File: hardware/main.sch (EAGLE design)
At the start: 104 parts, among them IC1 MPU-6050, IC2 TB6612FNG, M1 MOTOR_MOUNT_V2, M2 LED_MOUNT, M3 LED_MOUNT, M4 LED_MOUNT, M5 LED_MOUNT, M6 LED_MOUNT, M7 LED_MOUNT, Q7 IRLML2244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

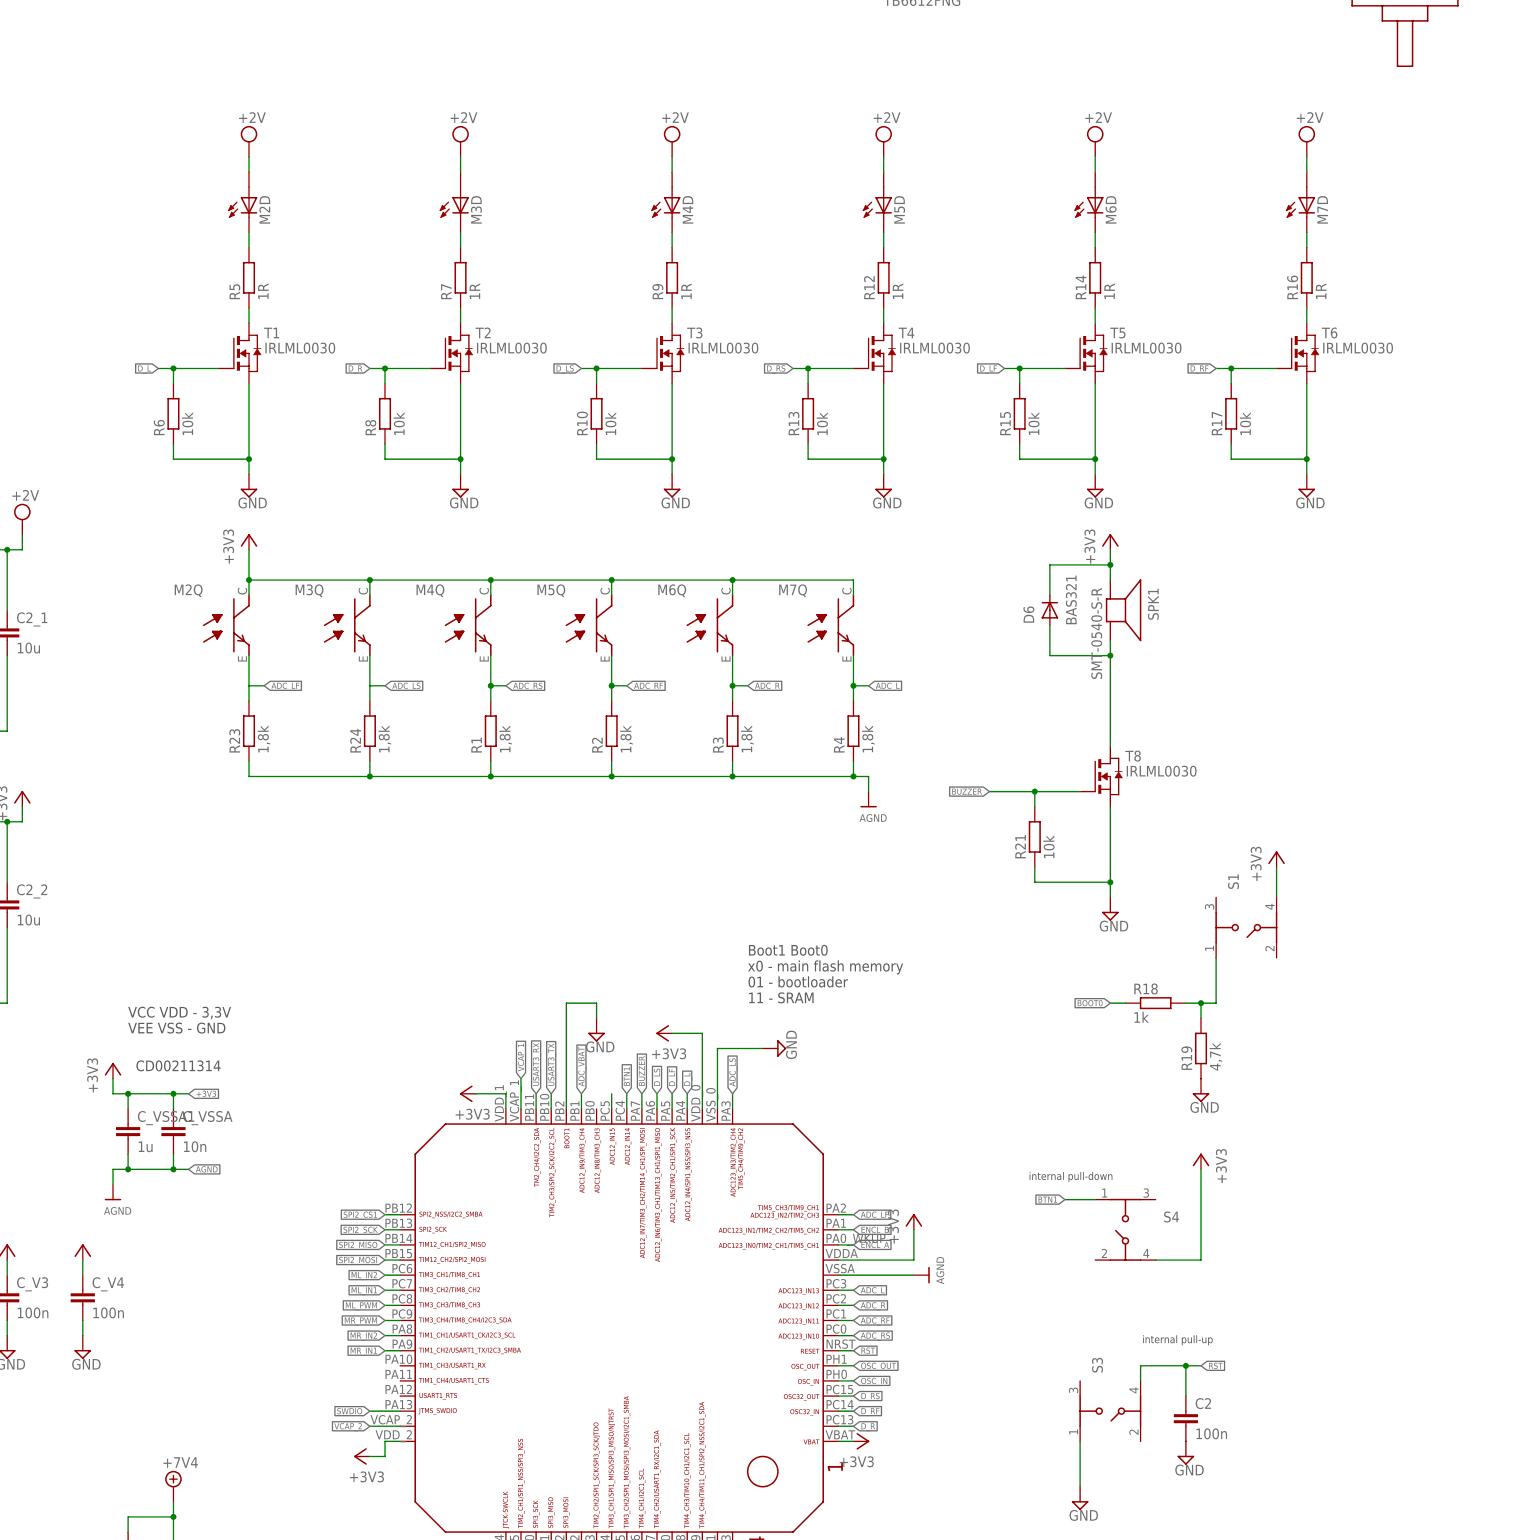
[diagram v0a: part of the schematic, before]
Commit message: Rozmieszczone diody na dziobie, przelotki przy DCDC
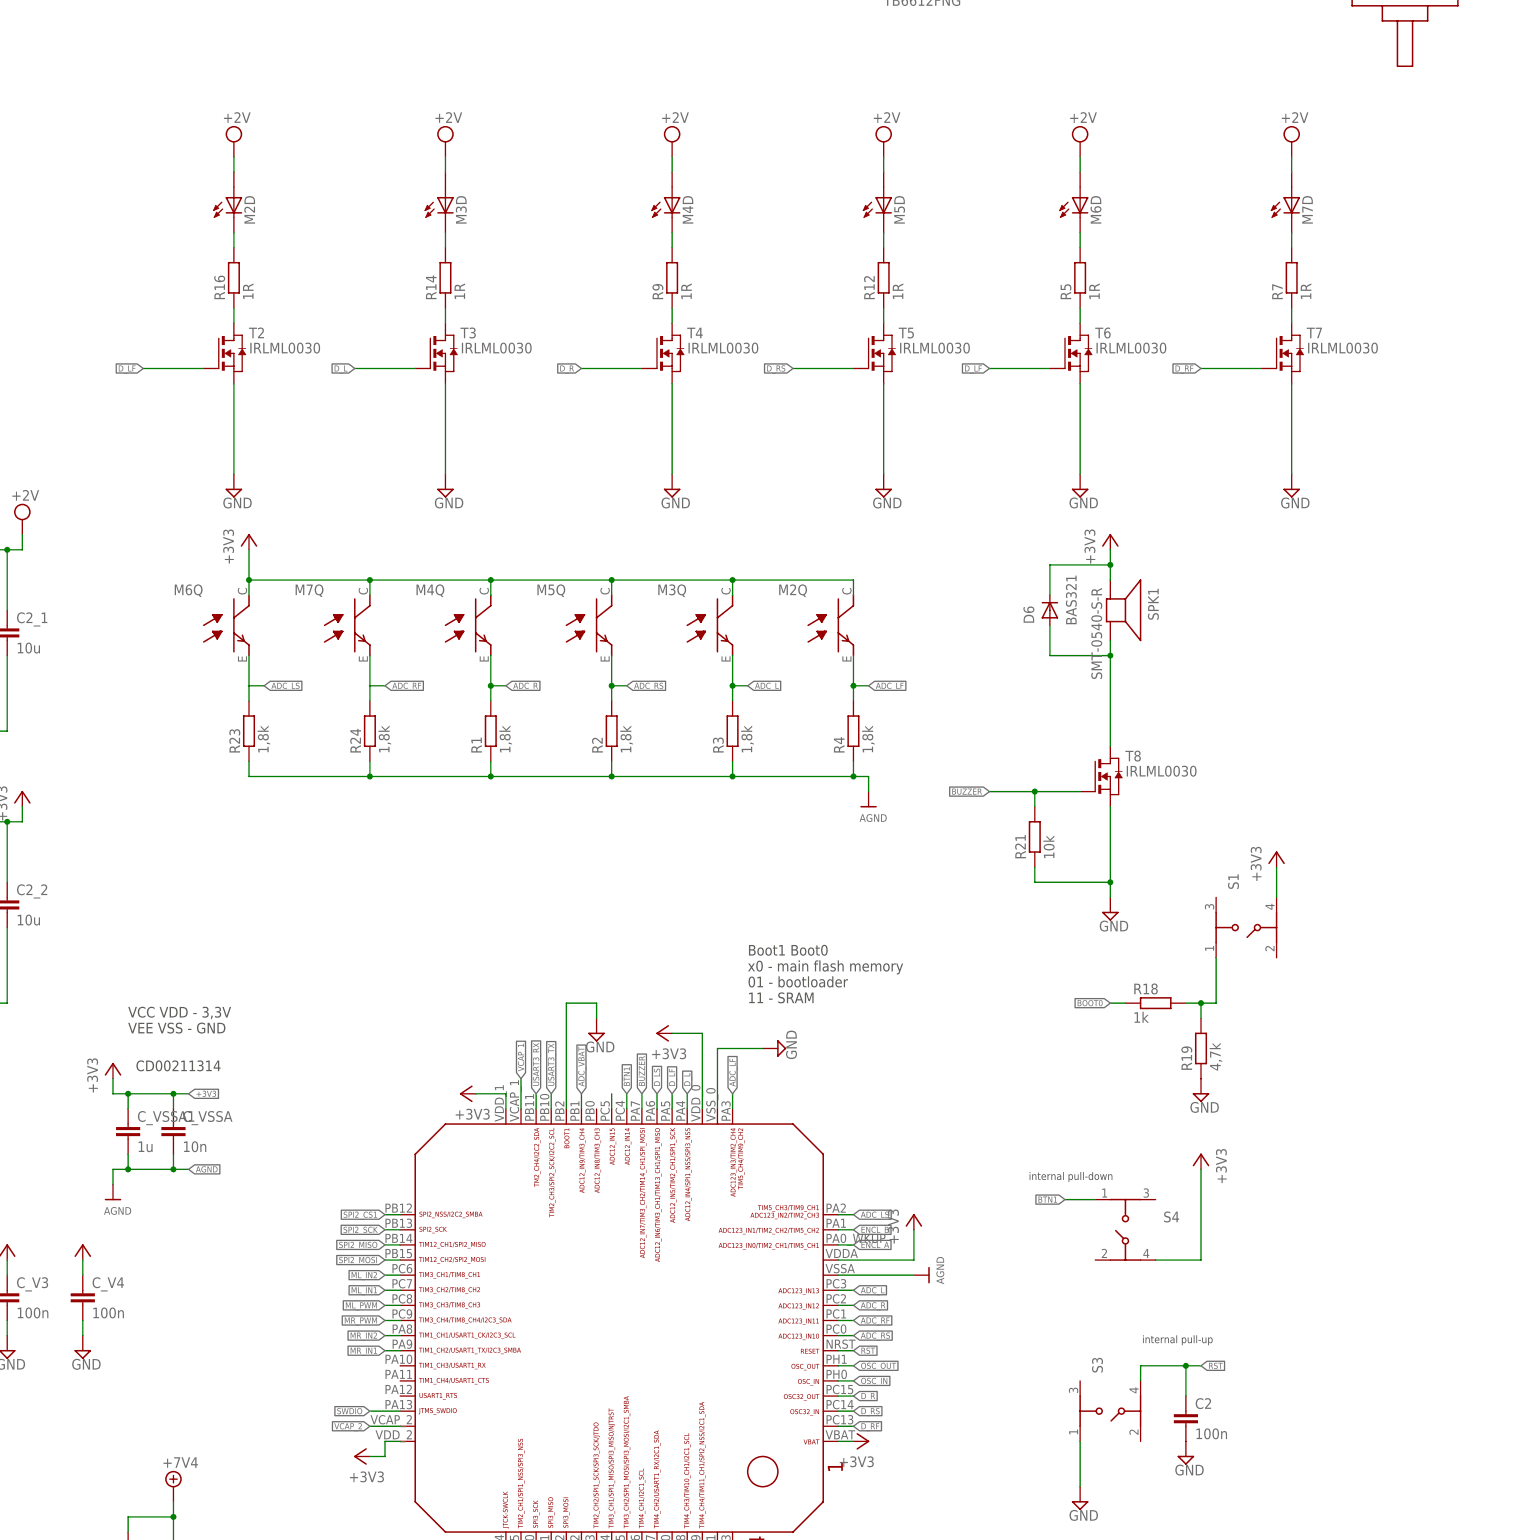
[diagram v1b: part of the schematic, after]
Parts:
- removed R10, R13, R15, R17, R6, R8: 10k, rcl:R-EU_R0603
- removed T1: IRLML0030, zetex:NMOSSOT23
- added T7: IRLML0030, zetex:NMOSSOT23
- renumbered U$1 to ON
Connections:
- net ADC_L: now also M3Q.E, R3.2; no longer M7Q.E, R4.2
- net ADC_LF: now also R4.2, U$6.PA3; no longer R23.2, U$6.PA2
- net ADC_LS: now also M6Q.E, R23.2, U$6.PA2; no longer M3Q.E, R24.2, U$6.PA3
- net ADC_R: now also M4Q.E, R1.2; no longer M6Q.E, R3.2
- net ADC_RF: now also M7Q.E, R24.2; no longer M5Q.E, R2.2
- net ADC_RS: now also M5Q.E, R2.2; no longer M4Q.E, R1.2
- net D_L: now also T3.G; no longer R6.2, T1.G
- net D_LF: now also T2.G, T6.G; no longer R15.2, T5.G
- net D_LS: no longer R10.2, T3.G
- net D_R: now also T4.G, U$6.PC15; no longer R8.2, T2.G, U$6.PC13
- net D_RF: now also T7.G, U$6.PC13; no longer R17.2, T6.G, U$6.PC14
- net D_RS: now also T5.G, U$6.PC14; no longer R13.2, T4.G, U$6.PC15
- net GND: now also T7.S; no longer R10.1, R13.1, R15.1, R17.1, R6.1, R8.1, T1.S
- net N$1: now also M7D.C; no longer M3D.C
- net N$10: now also M3D.C; no longer M6D.C
- net N$11: now also T3.D; no longer T5.D
- net N$12: now also M2D.C; no longer M7D.C
- net N$13: now also T2.D; no longer T6.D
- net N$3: now also M6D.C; no longer M2D.C
- net N$4: now also T6.D; no longer T1.D
- net N$5: now also T7.D; no longer T2.D
- net N$7: now also T4.D; no longer T3.D
- net N$9: now also T5.D; no longer T4.D
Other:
- moved on the sheet: M2D, M2Q, M3D, M3Q, M6D, M6Q, M7D, M7Q, R14, R16, R5, R7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

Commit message: 3d model - v1, gnd plane fun
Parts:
- removed LED6: blue, led:LEDSML1206
- removed R33: 33R, resistor:R-EU_R0805
- removed S2: (no value), EAGLE-TACT_SWITCHES-rev17c:450301014042
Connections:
- removed net LED5: LED6.C
- removed net N$25: LED6.A, R33.1
- removed net N$3: M6D.C, R5.2
- removed net OSC_IN: U$6.PH0
- new net N$2: M2D.C, R5.2
- net +3V3: no longer R33.2
- net ADC_RF: now also U$6.PC0; no longer U$6.PC1
- net ADC_RS: now also U$6.PC1; no longer U$6.PC0
- net D_LF: now also U$6.PA6; no longer T2.G, U$6.PA5
- net D_LS: now also T2.G, U$6.PA5; no longer U$6.PA6
- net LED4: now also U$6.PH0
- net N$12: now also M6D.C; no longer M2D.C
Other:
- moved on the sheet: M2D, M6D
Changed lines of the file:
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@@
 <part name="JP2" library="SparkFun_conn" deviceset="M02" device="POLAR"/>
 <part name="S1" library="EAGLE-TACT_SWITCHES-rev17c" deviceset="434153017835" device=""/>
-<part name="S2" library="EAGLE-TACT_SWITCHES-rev17c" deviceset="450301014042" device=""/>
 <part name="C5" library="rcl" deviceset="C-EU" device="C0603" value="10u"/>
 <part name="S3" library="EAGLE-TACT_SWITCHES-rev17c" deviceset="434153017835" device=""/>
@@
 <part name="R29" library="resistor" deviceset="R-EU_" device="R0805" value="33R"/>
 <part name="+3V26" library="supply1" deviceset="+3V3" device=""/>
-<part name="R33" library="resistor" deviceset="R-EU_" device="R0805" value="33R"/>
-<part name="LED6" library="led" deviceset="LED" device="SML1206" value="blue"/>
-<part name="+3V29" library="supply1" deviceset="+3V3" device=""/>
 <part name="C_V4" library="rcl" deviceset="C-EU" device="C0603" value="100n"/>
 <part name="AGND6" library="supply2" deviceset="GND" device=""/>
@@
 <instance part="AGND32" gate="GND" x="-124.46" y="142.24"/>
 <instance part="AGND33" gate="GND" x="-144.78" y="127"/>
-<instance part="SUPPLY2" gate="G$1" x="127" y="246.38"/>
+<instance part="SUPPLY2" gate="G$1" x="127" y="248.92"/>
 <instance part="SUPPLY9" gate="G$1" x="-50.8" y="182.88"/>
 <instance part="+3V8" gate="G$1" x="-50.8" y="137.16"/>
@@
 <instance part="T2" gate="A" x="-15.24" y="210.82"/>
 <instance part="AGND11" gate="GND" x="-15.24" y="187.96"/>
-<instance part="SUPPLY8" gate="G$1" x="-15.24" y="246.38"/>
+<instance part="SUPPLY8" gate="G$1" x="-15.24" y="248.92"/>
 <instance part="R21" gate="G$1" x="119.38" y="129.54" rot="R90"/>
 <instance part="U$7" gate="G$1" x="152.4" y="304.8"/>
@@
 <instance part="JP2" gate="G$1" x="-198.12" y="132.08"/>
 <instance part="S1" gate="G$1" x="154.94" y="114.3" rot="R90"/>
-<instance part="S2" gate="G$1" x="-195.58" y="71.12"/>
 <instance part="C5" gate="G$1" x="71.12" y="292.1" rot="R180"/>
 <instance part="S3" gate="G$1" x="132.08" y="33.02" rot="R90"/>
@@
 <instance part="R29" gate="G$1" x="66.04" y="-55.88" rot="R90"/>
 <instance part="+3V26" gate="G$1" x="66.04" y="-45.72"/>
-<instance part="R33" gate="G$1" x="88.9" y="-55.88" rot="R90"/>
-<instance part="LED6" gate="G$1" x="88.9" y="-68.58"/>
-<instance part="+3V29" gate="G$1" x="88.9" y="-45.72"/>
 <instance part="C_V4" gate="G$1" x="-40.64" y="53.34"/>
 <instance part="AGND6" gate="GND" x="-40.64" y="43.18"/>
@@
 <instance part="D9" gate="G$1" x="104.14" y="337.82" rot="R90"/>
 <instance part="M6" gate="Q" x="-15.24" y="165.1"/>
-<instance part="M6" gate="D" x="127" y="236.22"/>
+<instance part="M6" gate="D" x="-15.24" y="238.76"/>
 <instance part="M7" gate="Q" x="5.08" y="165.1"/>
 <instance part="M7" gate="D" x="162.56" y="236.22"/>
@@
 <instance part="M3" gate="D" x="20.32" y="236.22"/>
 <instance part="M2" gate="Q" x="86.36" y="165.1"/>
-<instance part="M2" gate="D" x="-15.24" y="236.22"/>
+<instance part="M2" gate="D" x="127" y="238.76"/>
 <instance part="L1" gate="A" x="243.84" y="292.1"/>
 <instance part="AGND36" gate="GND" x="45.72" y="96.52"/>
@@
 <net name="ADC_RF" class="0">
 <segment>
-<wire x1="86.36" y1="48.26" x2="88.9" y2="48.26" width="0.1524" layer="91"/>
-<label x="88.9" y="48.26" size="1.016" layer="95" xref="yes"/>
-<pinref part="U$6" gate="G$1" pin="PC1"/>
-</segment>
-<segment>
 <pinref part="R24" gate="G$1" pin="2"/>
 <wire x1="7.62" y1="160.02" x2="7.62" y2="154.94" width="0.1524" layer="91"/>
@@
 <pinref part="M7" gate="Q" pin="E"/>
 </segment>
-</net>
-<net name="ADC_RS" class="0">
 <segment>
 <wire x1="86.36" y1="45.72" x2="88.9" y2="45.72" width="0.1524" layer="91"/>
@@
 <pinref part="U$6" gate="G$1" pin="PC0"/>
 </segment>
+</net>
+<net name="ADC_RS" class="0">
 <segment>
 <pinref part="R2" gate="G$1" pin="2"/>
@@
 <label x="50.8" y="154.94" size="1.016" layer="95" xref="yes"/>
 <pinref part="M5" gate="Q" pin="E"/>
+</segment>
+<segment>
+<wire x1="86.36" y1="48.26" x2="88.9" y2="48.26" width="0.1524" layer="91"/>
+<label x="88.9" y="48.26" size="1.016" layer="95" xref="yes"/>
+<pinref part="U$6" gate="G$1" pin="PC1"/>
 </segment>
 </net>
@@
 <net name="D_LS" class="0">
 <segment>
-<pinref part="U$6" gate="G$1" pin="PA6"/>
-<wire x1="55.88" y1="83.82" x2="55.88" y2="86.36" width="0.1524" layer="91"/>
-<label x="55.88" y="86.36" size="1.016" layer="95" rot="R90" xref="yes"/>
+<label x="-30.48" y="208.28" size="1.016" layer="95" rot="R180" xref="yes"/>
+<pinref part="T2" gate="A" pin="G"/>
+<wire x1="-20.32" y1="208.28" x2="-30.48" y2="208.28" width="0.1524" layer="91"/>
+</segment>
+<segment>
+<pinref part="U$6" gate="G$1" pin="PA5"/>
+<wire x1="58.42" y1="83.82" x2="58.42" y2="86.36" width="0.1524" layer="91"/>
+<label x="58.42" y="86.36" size="1.016" layer="95" rot="R90" xref="yes"/>
 </segment>
 </net>
@@
 </segment>
 <segment>
-<pinref part="+3V29" gate="G$1" pin="+3V3"/>
-<pinref part="R33" gate="G$1" pin="2"/>
-<wire x1="88.9" y1="-48.26" x2="88.9" y2="-50.8" width="0.1524" layer="91"/>
-</segment>
-<segment>
 <pinref part="C_V4" gate="G$1" pin="1"/>
 <wire x1="-40.64" y1="55.88" x2="-40.64" y2="58.42" width="0.1524" layer="91"/>
@@
 <label x="144.78" y="-7.62" size="1.016" layer="95" xref="yes"/>
 <label x="144.78" y="-10.16" size="1.016" layer="95" xref="yes"/>
-</segment>
-</net>
-<net name="OSC_IN" class="0">
-<segment>
-<wire x1="86.36" y1="38.1" x2="88.9" y2="38.1" width="0.1524" layer="91"/>
-<label x="88.9" y="38.1" size="1.016" layer="95" xref="yes"/>
-<pinref part="U$6" gate="G$1" pin="PH0"/>
 </segment>
 </net>
@@
 <net name="D_LF" class="0">
 <segment>
-<pinref part="U$6" gate="G$1" pin="PA5"/>
-<wire x1="58.42" y1="83.82" x2="58.42" y2="86.36" width="0.1524" layer="91"/>
-<label x="58.42" y="86.36" size="1.016" layer="95" rot="R90" xref="yes"/>
-</segment>
-<segment>
-<label x="-30.48" y="208.28" size="1.016" layer="95" rot="R180" xref="yes"/>
-<pinref part="T2" gate="A" pin="G"/>
-<wire x1="-20.32" y1="208.28" x2="-30.48" y2="208.28" width="0.1524" layer="91"/>
-</segment>
-<segment>
 <label x="111.76" y="208.28" size="1.016" layer="95" rot="R180" xref="yes"/>
 <pinref part="T6" gate="A" pin="G"/>
 <wire x1="121.92" y1="208.28" x2="111.76" y2="208.28" width="0.1524" layer="91"/>
+</segment>
+<segment>
+<pinref part="U$6" gate="G$1" pin="PA6"/>
+<wire x1="55.88" y1="83.82" x2="55.88" y2="86.36" width="0.1524" layer="91"/>
+<label x="55.88" y="86.36" size="1.016" layer="95" rot="R90" xref="yes"/>
 </segment>
 </net>
@@
 <pinref part="S1" gate="G$1" pin="1"/>
 <wire x1="149.86" y1="101.6" x2="149.86" y2="109.22" width="0.1524" layer="91"/>
-</segment>
-</net>
-<net name="N$3" class="0">
-<segment>
-<wire x1="127" y1="231.14" x2="127" y2="228.6" width="0.1524" layer="91"/>
-<pinref part="R5" gate="G$1" pin="2"/>
-<pinref part="M6" gate="D" pin="C"/>
 </segment>
 </net>
@@
 <net name="VCC" class="0">
 <segment>
-<wire x1="127" y1="241.3" x2="127" y2="243.84" width="0.1524" layer="91"/>
-<pinref part="SUPPLY2" gate="G$1" pin="VCC"/>
-<pinref part="M6" gate="D" pin="A"/>
-</segment>
-<segment>
 <pinref part="R1_1" gate="G$1" pin="2"/>
 <wire x1="-60.96" y1="175.26" x2="-60.96" y2="177.8" width="0.1524" layer="91"/>
@@
 </segment>
 <segment>
-<wire x1="-15.24" y1="241.3" x2="-15.24" y2="243.84" width="0.1524" layer="91"/>
+<pinref part="SUPPLY2" gate="G$1" pin="VCC"/>
+<pinref part="M2" gate="D" pin="A"/>
+<wire x1="127" y1="246.38" x2="127" y2="243.84" width="0.1524" layer="91"/>
+</segment>
+<segment>
+<pinref part="M6" gate="D" pin="A"/>
 <pinref part="SUPPLY8" gate="G$1" pin="VCC"/>
-<pinref part="M2" gate="D" pin="A"/>
+<wire x1="-15.24" y1="246.38" x2="-15.24" y2="243.84" width="0.1524" layer="91"/>
 </segment>
 </net>
@@
 <net name="N$12" class="0">
 <segment>
-<wire x1="-15.24" y1="231.14" x2="-15.24" y2="228.6" width="0.1524" layer="91"/>
 <pinref part="R16" gate="G$1" pin="2"/>
-<pinref part="M2" gate="D" pin="C"/>
+<pinref part="M6" gate="D" pin="C"/>
+<wire x1="-15.24" y1="233.68" x2="-15.24" y2="228.6" width="0.1524" layer="91"/>
 </segment>
 </net>
@@
 </segment>
 </net>
-<net name="LED5" class="0">
-<segment>
-<pinref part="LED6" gate="G$1" pin="C"/>
-<wire x1="88.9" y1="-73.66" x2="88.9" y2="-76.2" width="0.1524" layer="91"/>
-<wire x1="88.9" y1="-76.2" x2="96.52" y2="-76.2" width="0.1524" layer="91"/>
-<label x="96.52" y="-76.2" size="1.27" layer="95" xref="yes"/>
-</segment>
-</net>
 <net name="LED4" class="0">
 <segment>
@@
 <label x="73.66" y="-76.2" size="1.27" layer="95" xref="yes"/>
 </segment>
+<segment>
+<wire x1="86.36" y1="38.1" x2="88.9" y2="38.1" width="0.1524" layer="91"/>
+<label x="88.9" y="38.1" size="1.016" layer="95" xref="yes"/>
+<pinref part="U$6" gate="G$1" pin="PH0"/>
+</segment>
 </net>
 <net name="N$24" class="0">
@@
 <pinref part="R29" gate="G$1" pin="1"/>
 <wire x1="66.04" y1="-60.96" x2="66.04" y2="-66.04" width="0.1524" layer="91"/>
-</segment>
-</net>
-<net name="N$25" class="0">
-<segment>
-<pinref part="R33" gate="G$1" pin="1"/>
-<pinref part="LED6" gate="G$1" pin="A"/>
-<wire x1="88.9" y1="-60.96" x2="88.9" y2="-66.04" width="0.1524" layer="91"/>
 </segment>
 </net>
@@
 </segment>
 </net>
+<net name="N$2" class="0">
+<segment>
+<pinref part="R5" gate="G$1" pin="2"/>
+<pinref part="M2" gate="D" pin="C"/>
+<wire x1="127" y1="233.68" x2="127" y2="228.6" width="0.1524" layer="91"/>
+</segment>
+</net>
